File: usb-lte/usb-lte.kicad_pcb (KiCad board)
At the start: 4 copper layers, 26 x 45 mm, 53 parts, among them J1 Sim Card, J2 Conn_Coaxial, J3 Conn_Coaxial, J4 Conn_Coaxial, J5 Conn_01x02_Pin, P1 USB_C_Plug_USB2.0, Q1 BC847W, Q2 BC847W, U1 AP2112K-3.3, U2 EG95

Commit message: Mark pi network caps as NC
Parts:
- C10, C11, C12, C13, C8, C9: value C_Small -> NC
- J1: value Sim Card -> Sim slot
- L1, L2, L3: value L_Small -> 0
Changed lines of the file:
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@@
 			)
 		)
-		(property "Value" "C_Small"
+		(property "Value" "NC"
 			(at 0 1.16 0)
 			(layer "F.Fab")
@@
 		(sheetname "EG95")
 		(sheetfile "eg95.kicad_sch")
-		(attr smd)
+		(attr smd dnp)
 		(fp_line
 			(start -0.107836 -0.36)
@@
 			)
 		)
-		(property "Value" "C_Small"
+		(property "Value" "NC"
 			(at 0 1.16 0)
 			(layer "F.Fab")
@@
 		(sheetname "EG95")
 		(sheetfile "eg95.kicad_sch")
-		(attr smd)
+		(attr smd dnp)
 		(fp_line
 			(start -0.107836 0.36)
@@
 			)
 		)
-		(property "Value" "C_Small"
+		(property "Value" "NC"
 			(at 0 1.16 0)
 			(layer "F.Fab")
@@
 		(sheetname "EG95")
 		(sheetfile "eg95.kicad_sch")
-		(attr smd)
+		(attr smd dnp)
 		(fp_line
 			(start -0.107836 0.36)
@@
 			)
 		)
-		(property "Value" "C_Small"
+		(property "Value" "NC"
 			(at 0 1.16 0)
 			(layer "F.Fab")
@@
 		(sheetname "EG95")
 		(sheetfile "eg95.kicad_sch")
-		(attr smd)
+		(attr smd dnp)
 		(fp_line
 			(start -0.107836 -0.36)
@@
 			)
 		)
-		(property "Value" "C_Small"
+		(property "Value" "NC"
 			(at 0 1.16 0)
 			(layer "F.Fab")
@@
 		(sheetname "EG95")
 		(sheetfile "eg95.kicad_sch")
-		(attr smd)
+		(attr smd dnp)
 		(fp_line
 			(start -0.107836 -0.36)
@@
 			)
 		)
-		(property "Value" "C_Small"
+		(property "Value" "NC"
 			(at 0 1.16 0)
 			(layer "F.Fab")
@@
 		(sheetname "EG95")
 		(sheetfile "eg95.kicad_sch")
-		(attr smd)
+		(attr smd dnp)
 		(fp_line
 			(start -0.107836 -0.36)
@@
 			)
 		)
-		(property "Value" "L_Small"
+		(property "Value" "0"
 			(at 0 1.17 90)
 			(layer "F.Fab")
@@
 			)
 		)
-		(property "Value" "L_Small"
+		(property "Value" "0"
 			(at 0 1.17 90)
 			(layer "F.Fab")
@@
 			)
 		)
-		(property "Value" "L_Small"
+		(property "Value" "0"
 			(at 0 1.17 90)
 			(layer "F.Fab")
@@
 		(tags "EG95EXGA-128-SGNS ")
 		(property "Reference" "U2"
-			(at -11.1 -15.6 0)
+			(at -11.375 -15.475 0)
 			(unlocked yes)
 			(layer "F.SilkS")
@@
 					(size 0.6 0.6)
 					(thickness 0.1)
+					(bold yes)
 				)
 			)
@@
 		(fp_text user "*"
 			(at -10.3815 -9.350001 180)
+			(unlocked yes)
 			(layer "F.SilkS")
 			(effects
@@
 		(fp_text user "*"
 			(at -10.3815 -9.350001 180)
-			(unlocked yes)
 			(layer "F.SilkS")
 			(effects
@@
 			)
 		)
-		(fp_text user "${REFERENCE}"
-			(at 0 0 180)
+		(fp_text user "*"
+			(at -7.9685 -9.350001 180)
 			(unlocked yes)
 			(layer "F.Fab")
@@
 			)
 		)
-		(fp_text user "*"
-			(at -7.9685 -9.350001 180)
+		(fp_text user "${REFERENCE}"
+			(at 0 0 180)
 			(unlocked yes)
 			(layer "F.Fab")
@@
 			)
 		)
-		(property "Value" "Sim Card"
+		(property "Value" "Sim slot"
 			(at 0 -1 90)
 			(unlocked yes)
@@
 		(tags "resistor handsolder")
 		(property "Reference" "R8"
-			(at -1.75 0 0)
+			(at -0.025 0.875 0)
 			(layer "B.SilkS")
 			(effects

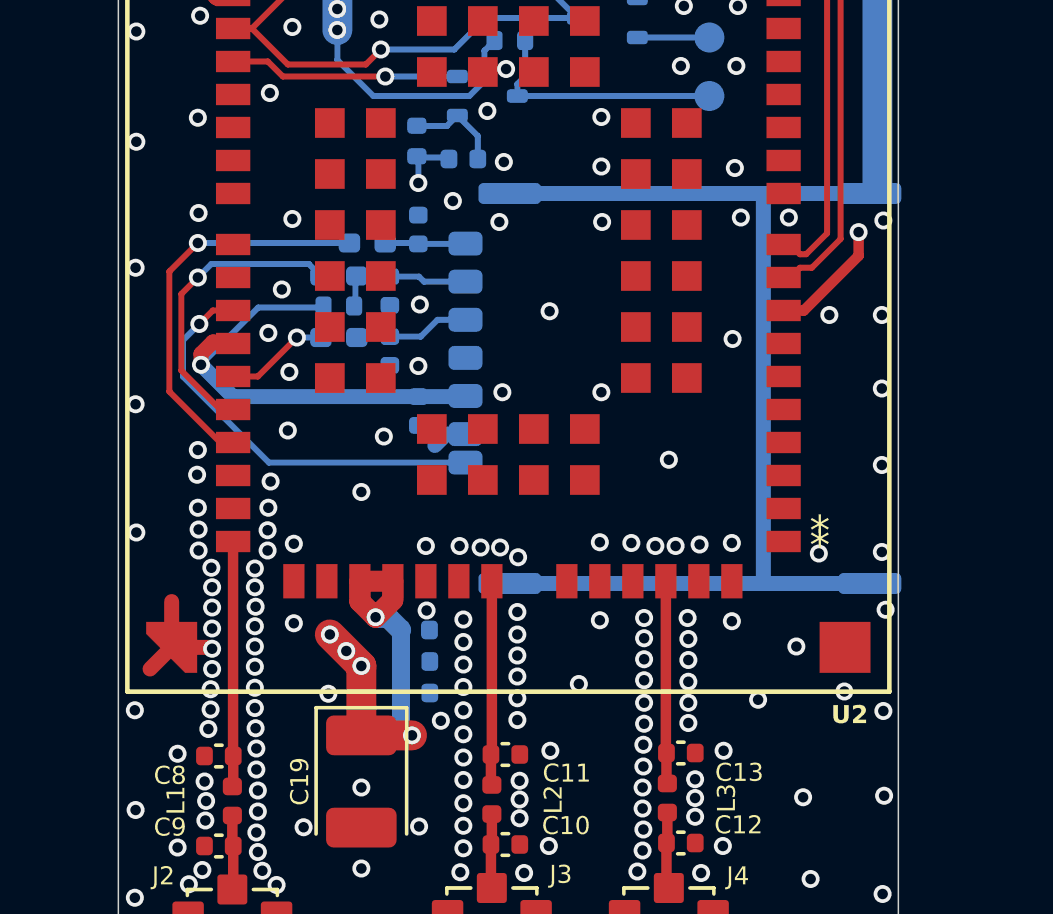
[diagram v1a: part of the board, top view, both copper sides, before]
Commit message: separate gnd and sim gnd
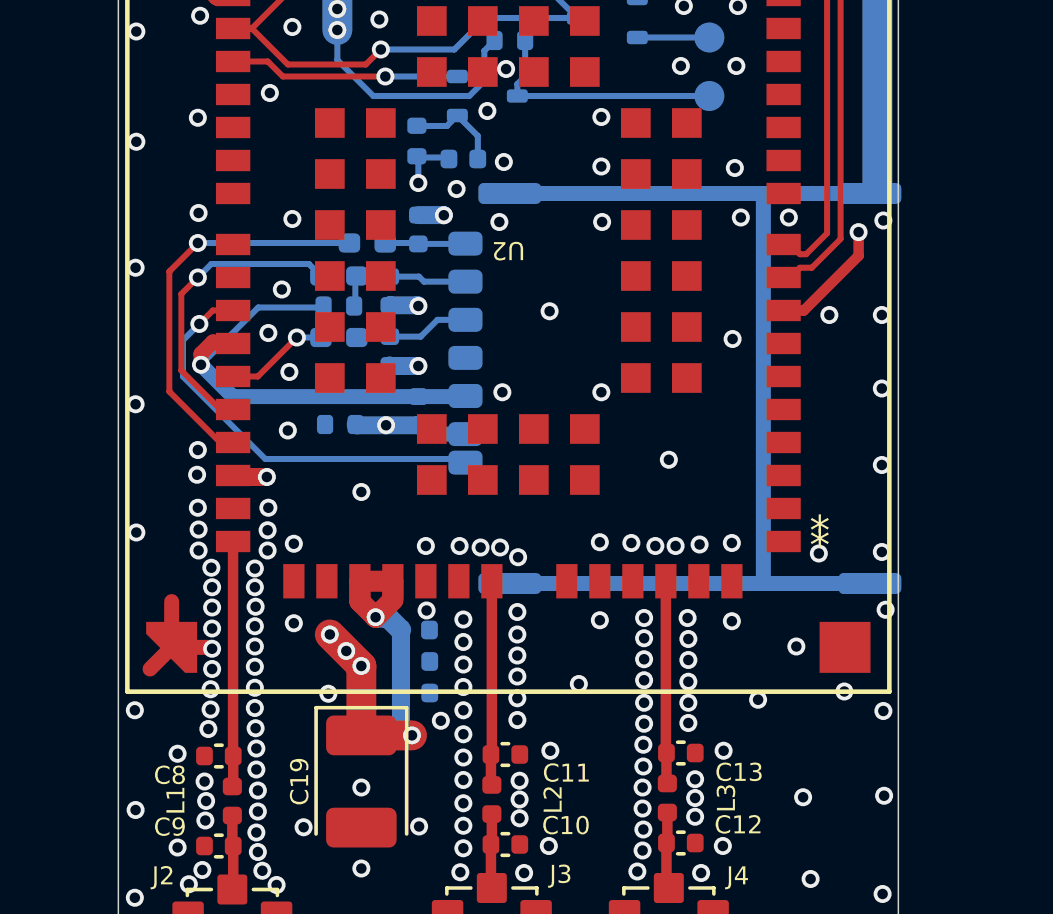
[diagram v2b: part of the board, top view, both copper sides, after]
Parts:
- added R4: 0, Resistor_SMD:R_0402_1005Metric, B.Cu at (145.0, 114.2)
- L1, L2, L3: value 0 -> 0R
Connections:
- C1 pad 2: MODEM_USIM_GND -> GND
- C10 pad 2: MODEM_USIM_GND -> GND
- C11 pad 2: MODEM_USIM_GND -> GND
- C12 pad 2: MODEM_USIM_GND -> GND
- C13 pad 2: MODEM_USIM_GND -> GND
- C16 pad 2: MODEM_USIM_GND -> GND
- C17 pad 2: MODEM_USIM_GND -> GND
- C18 pad 2: MODEM_USIM_GND -> GND
- C19 pad 2: MODEM_USIM_GND -> GND
- C2 pad 2: MODEM_USIM_GND -> GND
- C20 pad 2: MODEM_USIM_GND -> GND
- C21 pad 2: MODEM_USIM_GND -> GND
- C22 pad 2: MODEM_USIM_GND -> GND
- C23 pad 2: MODEM_USIM_GND -> GND
- C8 pad 2: MODEM_USIM_GND -> GND
- C9 pad 2: MODEM_USIM_GND -> GND
- D1 pad 1: MODEM_USIM_GND -> GND
- J2 pad 2: MODEM_USIM_GND -> GND
- J3 pad 2: MODEM_USIM_GND -> GND
- J4 pad 2: MODEM_USIM_GND -> GND
- J5 pad 2: MODEM_USIM_GND -> GND
- P1 pad A1: MODEM_USIM_GND -> GND
- P1 pad A12: MODEM_USIM_GND -> GND
- P1 pad B1: MODEM_USIM_GND -> GND
- P1 pad B12: MODEM_USIM_GND -> GND
- P1 pad S1: MODEM_USIM_GND -> GND
- R1 pad 2: MODEM_USIM_GND -> GND
- TP1 pad 1: MODEM_USIM_GND -> GND
- TP2 pad 1: MODEM_USIM_GND -> GND
- TP3 pad 1: MODEM_USIM_GND -> GND
- TP4 pad 1: MODEM_USIM_GND -> GND
- TP7 pad 1: MODEM_USIM_GND -> GND
- U1 pad 2: MODEM_USIM_GND -> GND
- U2 pad 100: MODEM_USIM_GND -> GND
- U2 pad 101: MODEM_USIM_GND -> GND
- U2 pad 102: MODEM_USIM_GND -> GND
- U2 pad 103: MODEM_USIM_GND -> GND
- U2 pad 104: MODEM_USIM_GND -> GND
- U2 pad 105: MODEM_USIM_GND -> GND
- U2 pad 106: MODEM_USIM_GND -> GND
- U2 pad 3: MODEM_USIM_GND -> GND
- U2 pad 31: MODEM_USIM_GND -> GND
- U2 pad 48: MODEM_USIM_GND -> GND
- U2 pad 50: MODEM_USIM_GND -> GND
- U2 pad 54: MODEM_USIM_GND -> GND
- U2 pad 55: MODEM_USIM_GND -> GND
- U2 pad 58: MODEM_USIM_GND -> GND
- U2 pad 59: MODEM_USIM_GND -> GND
- U2 pad 61: MODEM_USIM_GND -> GND
- U2 pad 62: MODEM_USIM_GND -> GND
- U2 pad 67: MODEM_USIM_GND -> GND
- U2 pad 68: MODEM_USIM_GND -> GND
- U2 pad 69: MODEM_USIM_GND -> GND
- U2 pad 70: MODEM_USIM_GND -> GND
- U2 pad 71: MODEM_USIM_GND -> GND
- U2 pad 72: MODEM_USIM_GND -> GND
- U2 pad 73: MODEM_USIM_GND -> GND
- U2 pad 74: MODEM_USIM_GND -> GND
- U2 pad 79: MODEM_USIM_GND -> GND
- U2 pad 80: MODEM_USIM_GND -> GND
- U2 pad 81: MODEM_USIM_GND -> GND
- U2 pad 82: MODEM_USIM_GND -> GND
- U2 pad 89: MODEM_USIM_GND -> GND
- U2 pad 90: MODEM_USIM_GND -> GND
- U2 pad 91: MODEM_USIM_GND -> GND
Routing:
- net GND: track 0.00 -> 15.5 mm, vias 0 -> 228
- net MODEM_USIM_GND: track 17.2 -> 20.7 mm, vias 232 -> 5
- added copper zone on B.Cu, net GND
- added copper zone on F.Cu, net GND
- added copper zone on In1.Cu, net GND
- removed copper zone on B.Cu, net MODEM_USIM_GND
- removed copper zone on F.Cu, net MODEM_USIM_GND
- removed copper zone on In1.Cu, net MODEM_USIM_GND

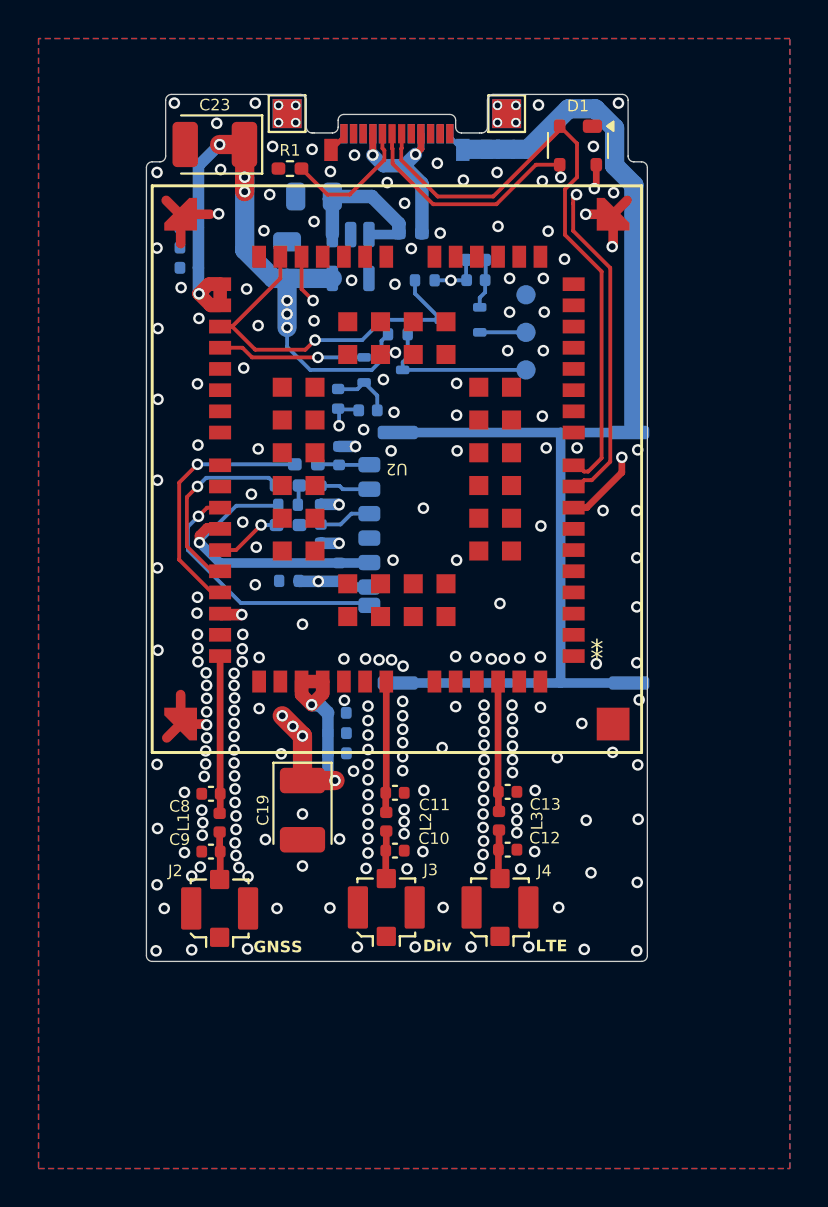
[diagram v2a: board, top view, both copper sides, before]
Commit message: added positioning NPTH for sim slot
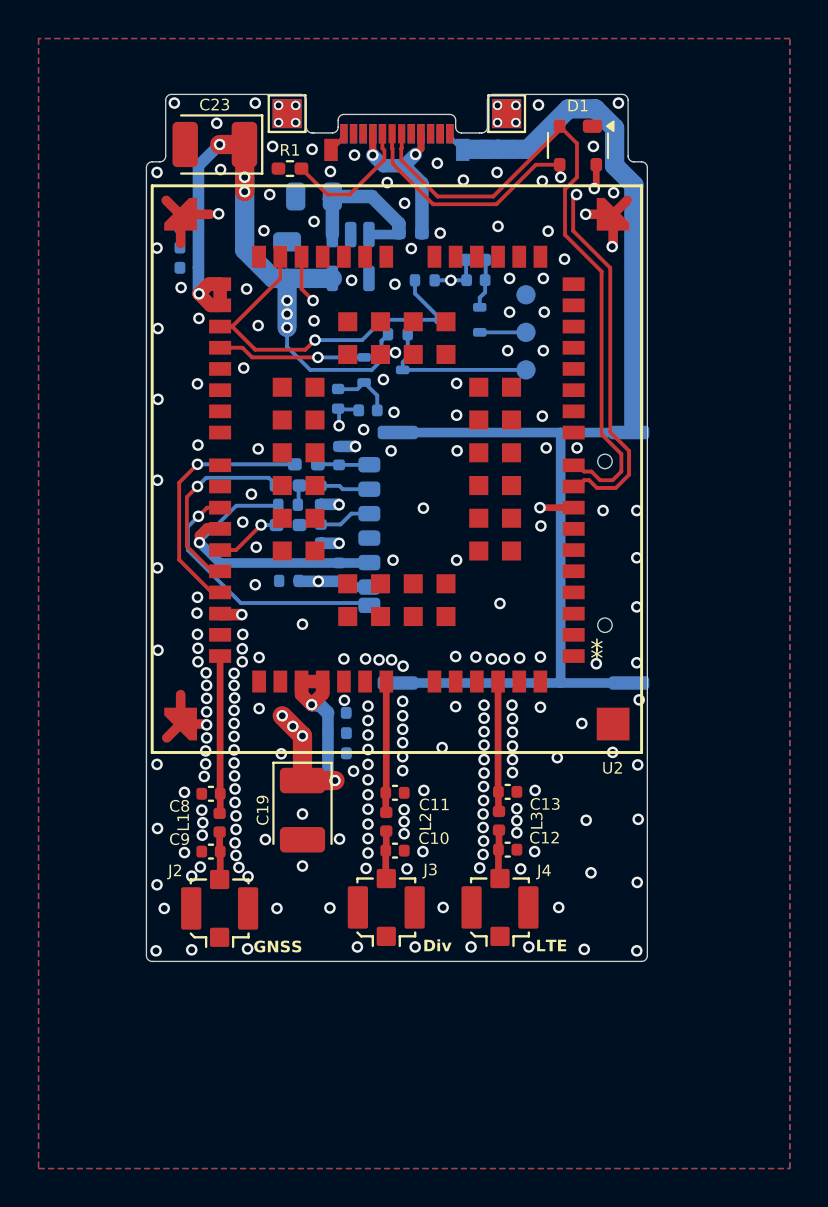
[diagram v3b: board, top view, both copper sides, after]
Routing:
- net USB_DN: track 32.5 -> 34.8 mm
- net USB_DP: track 31.0 -> 33.1 mm
- net VBUS: track 41.9 -> 43.0 mm
- net GND: vias 228 -> 227

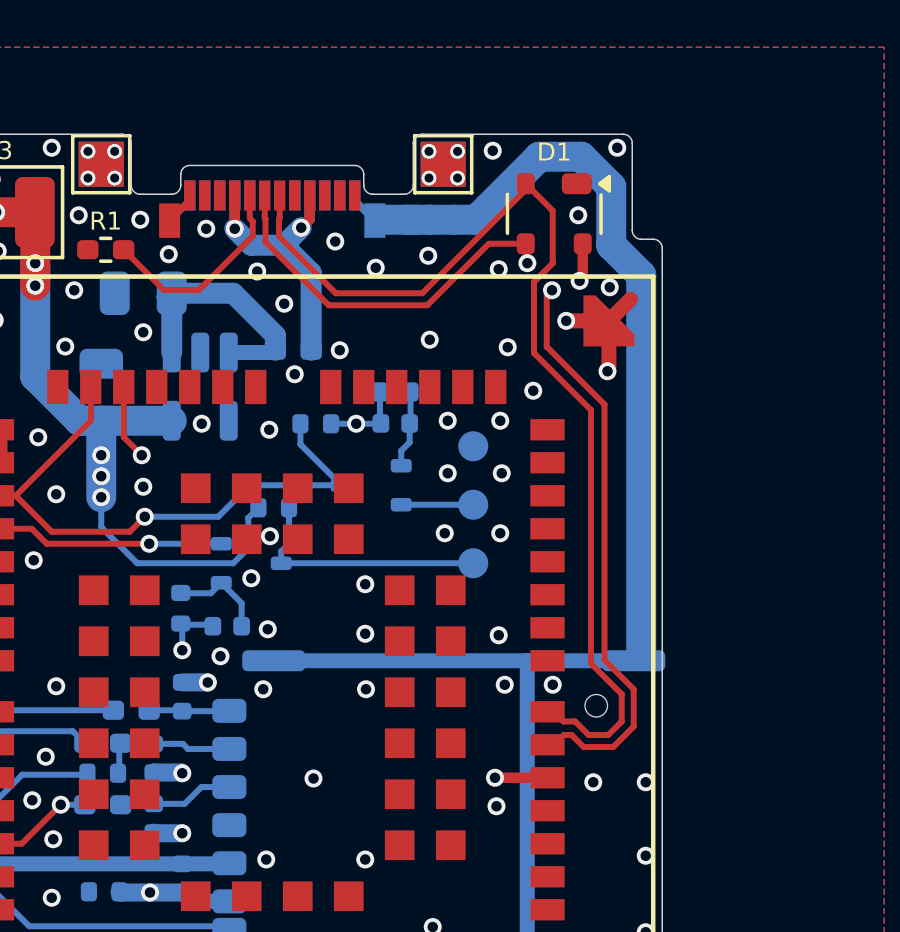
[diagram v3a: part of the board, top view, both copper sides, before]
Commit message: match usb 90 ohm impedance
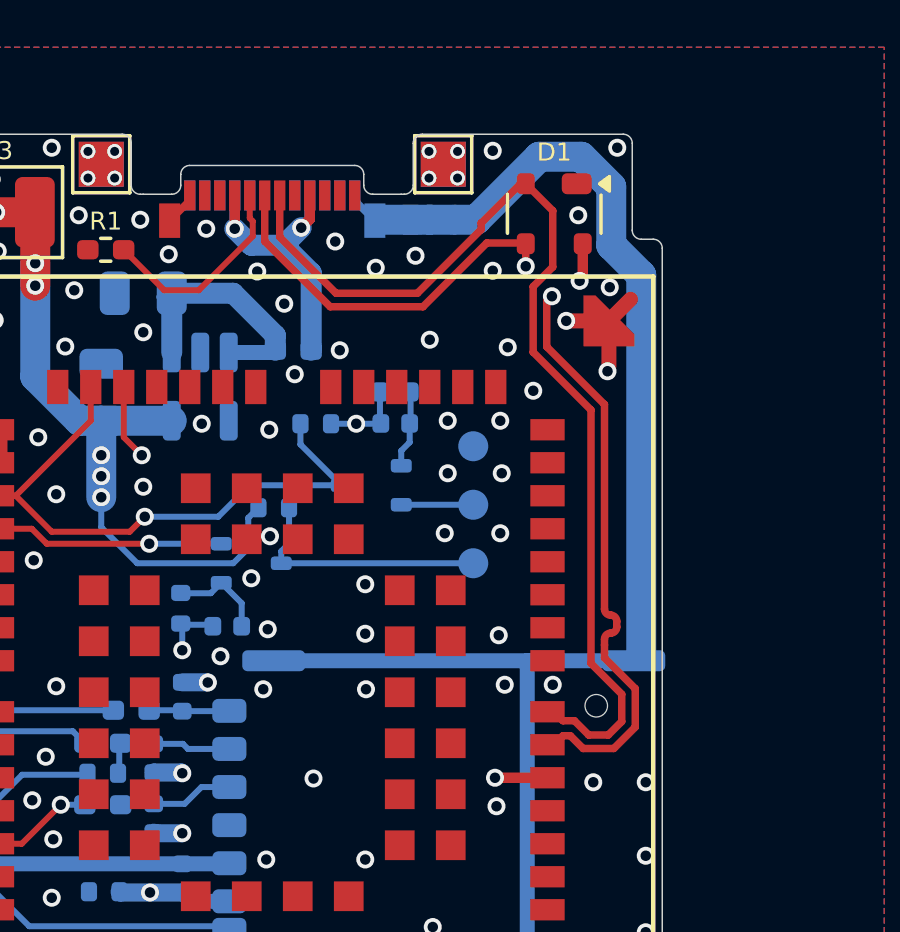
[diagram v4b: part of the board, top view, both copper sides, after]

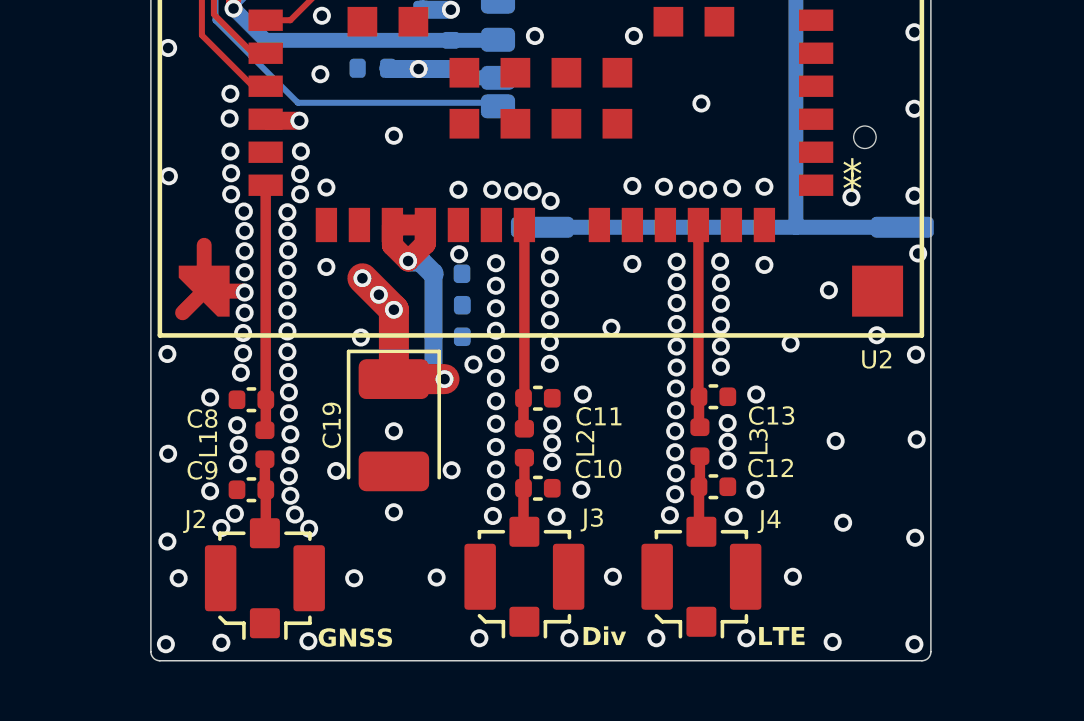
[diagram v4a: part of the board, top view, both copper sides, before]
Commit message: Use main power rail for gnss antenna
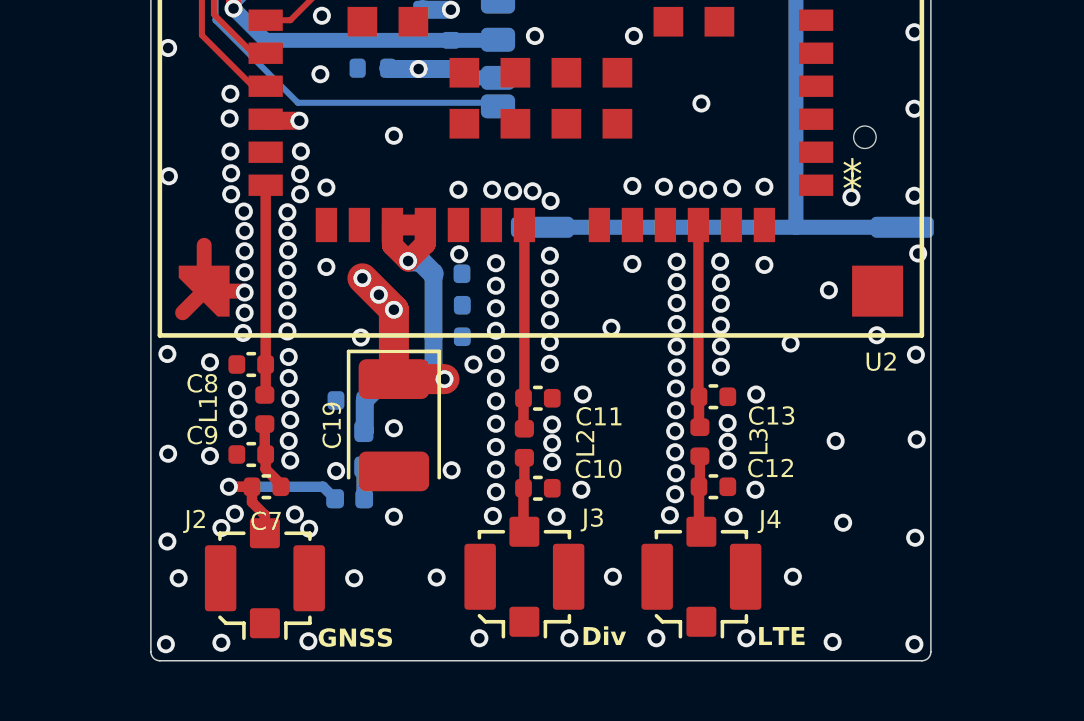
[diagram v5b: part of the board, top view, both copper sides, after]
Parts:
- added C24: 0.1uF, Capacitor_SMD:C_0402_1005Metric, B.Cu at (144.2, 125.2)
- added C7: 100pF, Capacitor_SMD:C_0402_1005Metric, F.Cu at (141.4, 128.1)
- added L4: 47nH, Inductor_SMD:L_0402_1005Metric, B.Cu at (144.2, 128.5)
- added R5: 10, Resistor_SMD:R_0402_1005Metric_Pad0.72x0.64mm_HandSolder, B.Cu at (144.7, 126.8)
- moved C8 1.18 mm to (140.9, 124.0)
- moved L1 1.18 mm to (141.4, 125.5)
- moved C9 1.18 mm to (140.9, 127.0)
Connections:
- C9 pad 1: Net-(J2-In) -> Net-(C7-Pad1)
- L1 pad 2: Net-(J2-In) -> Net-(C7-Pad1)
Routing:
- net +3V3: track 72.3 -> 76.3 mm
- net Net-(J2-In): track 2.49 -> 6.25 mm, vias 0 -> 1
- net Net-(C7-Pad1): track 0.00 -> 2.31 mm
- net Net-(U2A-ANT_GNSS/ANT_DIV): track 8.18 -> 7.01 mm
- net Net-(L4-Pad1): track 0.00 -> 1.13 mm
- net GND: vias 227 -> 223
